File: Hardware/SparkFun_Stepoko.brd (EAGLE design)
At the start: 150 x 82 mm, 184 parts, among them J1 AVR ISP, Q1 16MHZ, Q2 100A/100V, U1 ATMEGA328, U10 +12v, U2 FT232RLSSOP, U3 74LVC1G04, U4 LM25011, U5 DRV8811, U6 74HC7014D, U7 7432SE, U8 DRV8811, U9 DRV8811

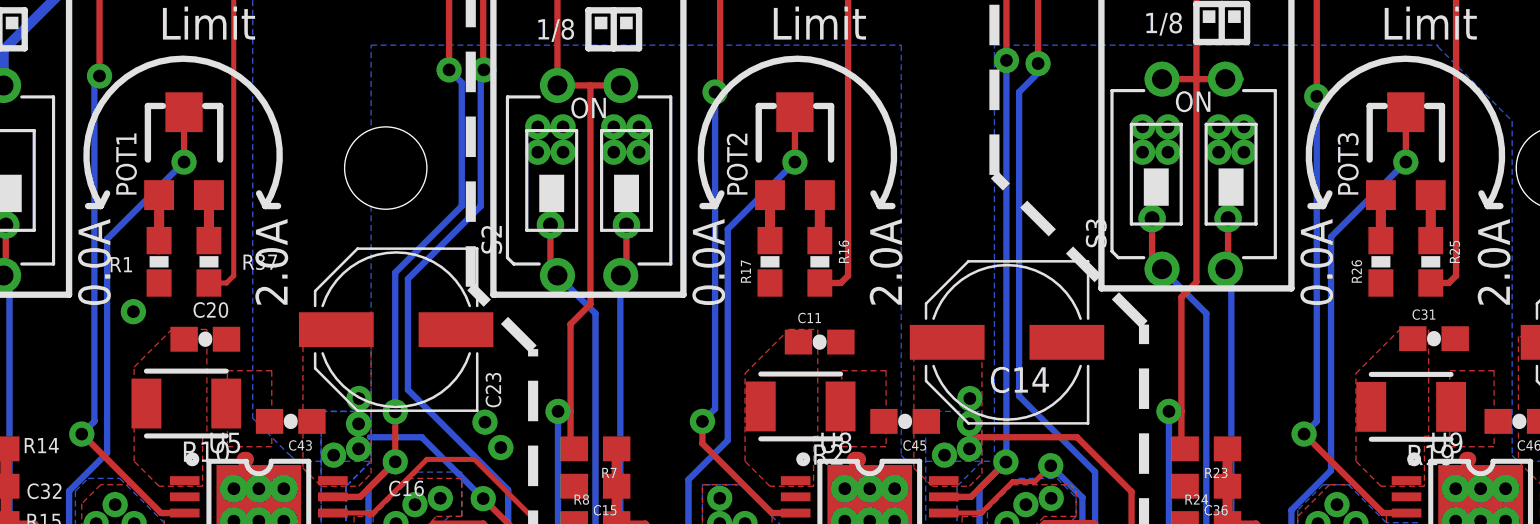
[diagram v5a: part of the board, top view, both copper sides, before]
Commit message: fixed current limit resistor values
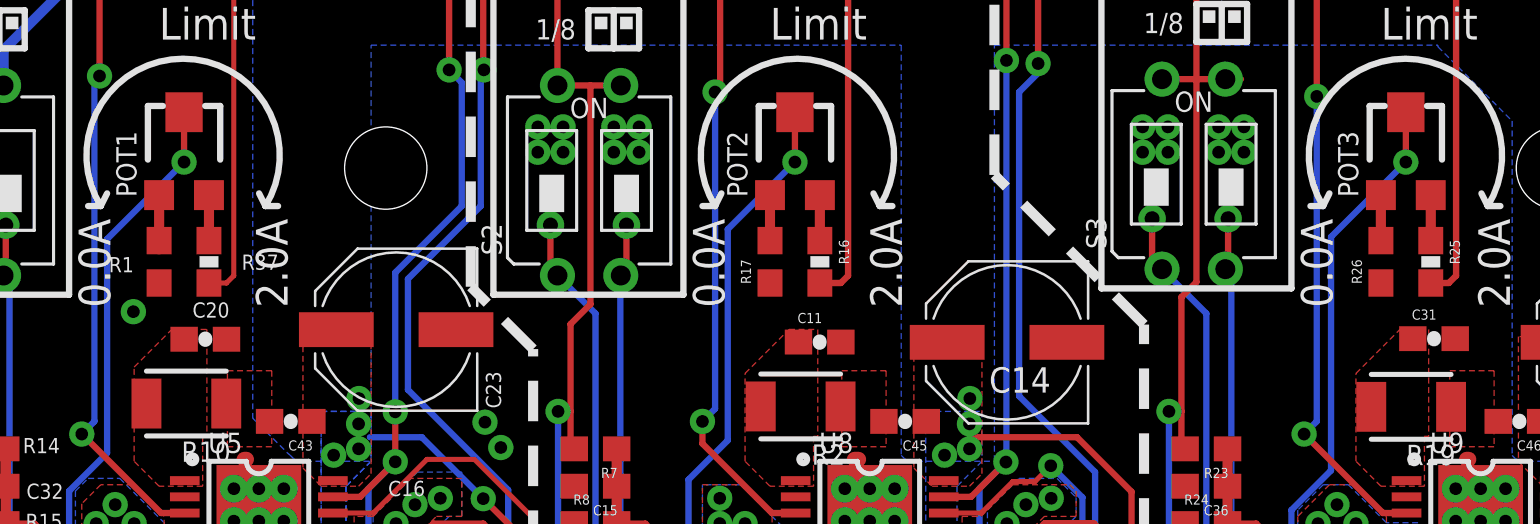
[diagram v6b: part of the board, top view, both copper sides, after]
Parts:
- R1, R17, R26: value 240 -> 0; device SparkFun-Resistors:0603-RES -> SparkFun-Resistors:0603
- R16, R25, R37: value 1K -> 3.3K
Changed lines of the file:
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@@
 <attribute name="PROD_ID" value="CAP-12380" x="5.5" y="35.5" size="1.778" layer="27" rot="R180" display="off"/>
 </element>
-<element name="R37" library="SparkFun-Resistors" package="0603-RES" value="1K" x="14.5" y="44.5" smashed="yes" rot="R270">
+<element name="R37" library="SparkFun-Resistors" package="0603-RES" value="3.3K" x="14.5" y="44.5" smashed="yes" rot="R270">
 <attribute name="NAME" x="17.2922" y="44.7903" size="0.6096" layer="25" rot="R180"/>
-<attribute name="VALUE" value="1K" x="13.992" y="46.024" size="0.4064" layer="27"/>
-<attribute name="PROD_ID" value="RES-07856" x="14.5" y="44.5" size="1.778" layer="27" rot="R270" display="off"/>
+<attribute name="PROD_ID" value="RES-07851" x="14.5" y="44.5" size="1.778" layer="27" rot="R270" display="off"/>
 </element>
 <element name="C44" library="SparkFun-Capacitors" package="0603-CAP" value="0.1uF" x="5.5" y="26.5" smashed="yes" rot="R180">
@@
 <attribute name="PROD_ID" value="RES-12428" x="13.5" y="49" size="1.778" layer="27" display="off"/>
 </element>
-<element name="R1" library="SparkFun-Resistors" package="0603-RES" value="240" x="12.5" y="44.5" smashed="yes" rot="R90">
+<element name="R1" library="SparkFun-Resistors" package="0603" value="0" x="12.5" y="44.5" smashed="yes" rot="R90">
 <attribute name="NAME" x="11.484" y="44.6905" size="0.6096" layer="25" rot="R180"/>
-<attribute name="PROD_ID" value="RES-07849" x="12.5" y="44.5" size="1.778" layer="27" rot="R90" display="off"/>
-<attribute name="VALUE" value="240" x="12.5" y="44.5" size="1.778" layer="27" rot="R90" display="off"/>
+<attribute name="PROD_ID" value="RES-08609" x="12.5" y="44.5" size="1.778" layer="27" rot="R90" display="off"/>
+<attribute name="VALUE" value="0" x="12.5" y="44.5" size="1.778" layer="27" rot="R90" display="off"/>
 </element>
 <element name="R6" library="SparkFun-Resistors" package="0603-RES" value="10K" x="129.5" y="41">
@@
 <attribute name="PROD_ID" value="CAP-12380" x="30" y="35.5" size="1.778" layer="27" rot="R180" display="off"/>
 </element>
-<element name="R16" library="SparkFun-Resistors" package="0603-RES" value="1K" x="39" y="44.5" rot="R270">
-<attribute name="PROD_ID" value="RES-07856" x="39" y="44.5" size="1.778" layer="27" rot="R270" display="off"/>
-<attribute name="VALUE" value="1K" x="39" y="44.5" size="1.778" layer="27" rot="R270" display="off"/>
+<element name="R16" library="SparkFun-Resistors" package="0603-RES" value="3.3K" x="39" y="44.5" rot="R270">
+<attribute name="PROD_ID" value="RES-07851" x="39" y="44.5" size="1.778" layer="27" rot="R270" display="off"/>
 </element>
 <element name="C24" library="SparkFun-Capacitors" package="0603-CAP" value="0.1uF" x="30" y="26.5" rot="R180">
@@
 <attribute name="PROD_ID" value="RES-12428" x="38" y="49" size="1.778" layer="27" display="off"/>
 </element>
-<element name="R17" library="SparkFun-Resistors" package="0603-RES" value="240" x="37" y="44.5" rot="R90">
-<attribute name="PROD_ID" value="RES-07849" x="37" y="44.5" size="1.778" layer="27" rot="R90" display="off"/>
-<attribute name="VALUE" value="240" x="37" y="44.5" size="1.778" layer="27" rot="R90" display="off"/>
+<element name="R17" library="SparkFun-Resistors" package="0603" value="0" x="37" y="44.5" rot="R90">
+<attribute name="PROD_ID" value="RES-08609" x="37" y="44.5" size="1.778" layer="27" rot="R90" display="off"/>
+<attribute name="VALUE" value="0" x="37" y="44.5" size="1.778" layer="27" rot="R90" display="off"/>
 </element>
 <element name="Y-A" library="SparkFun-Connectors" package="SCREWTERMINAL-3.5MM-2_LOCK" value="3.5mm" x="41" y="11.5">
@@
 <attribute name="PROD_ID" value="CAP-12380" x="54.5" y="35.5" size="1.778" layer="27" rot="R180" display="off"/>
 </element>
-<element name="R25" library="SparkFun-Resistors" package="0603-RES" value="1K" x="63.5" y="44.5" rot="R270">
-<attribute name="PROD_ID" value="RES-07856" x="63.5" y="44.5" size="1.778" layer="27" rot="R270" display="off"/>
-<attribute name="VALUE" value="1K" x="63.5" y="44.5" size="1.778" layer="27" rot="R270" display="off"/>
+<element name="R25" library="SparkFun-Resistors" package="0603-RES" value="3.3K" x="63.5" y="44.5" rot="R270">
+<attribute name="PROD_ID" value="RES-07851" x="63.5" y="44.5" size="1.778" layer="27" rot="R270" display="off"/>
 </element>
 <element name="C37" library="SparkFun-Capacitors" package="0603-CAP" value="0.1uF" x="54.5" y="26.5" rot="R180">
@@
 <attribute name="PROD_ID" value="RES-12428" x="62.5" y="49" size="1.778" layer="27" display="off"/>
 </element>
-<element name="R26" library="SparkFun-Resistors" package="0603-RES" value="240" x="61.5" y="44.5" rot="R90">
-<attribute name="PROD_ID" value="RES-07849" x="61.5" y="44.5" size="1.778" layer="27" rot="R90" display="off"/>
-<attribute name="VALUE" value="240" x="61.5" y="44.5" size="1.778" layer="27" rot="R90" display="off"/>
+<element name="R26" library="SparkFun-Resistors" package="0603" value="0" x="61.5" y="44.5" rot="R90">
+<attribute name="PROD_ID" value="RES-08609" x="61.5" y="44.5" size="1.778" layer="27" rot="R90" display="off"/>
+<attribute name="VALUE" value="0" x="61.5" y="44.5" size="1.778" layer="27" rot="R90" display="off"/>
 </element>
 <element name="Z-A" library="SparkFun-Connectors" package="SCREWTERMINAL-3.5MM-2_LOCK" value="3.5mm" x="55" y="11.5">
